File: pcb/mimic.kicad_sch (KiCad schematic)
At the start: 10 parts

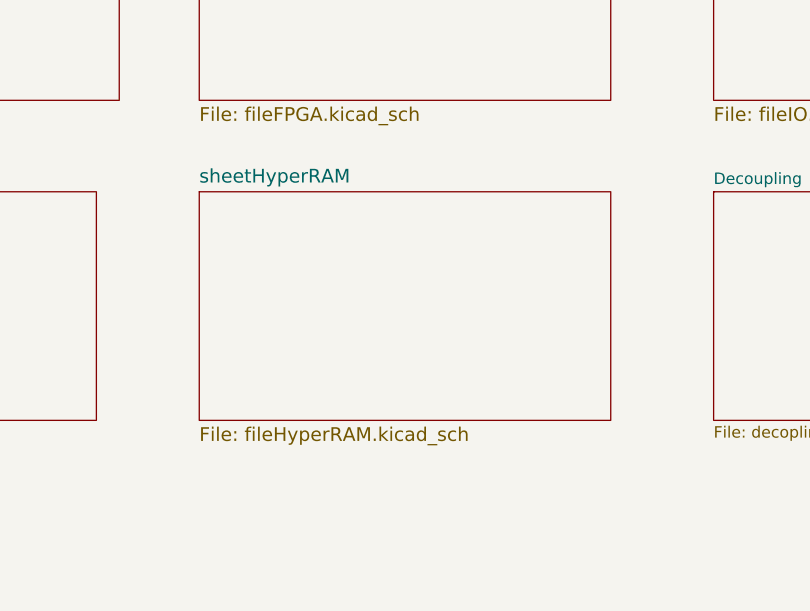
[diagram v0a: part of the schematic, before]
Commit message: refactor(pcb): strip down
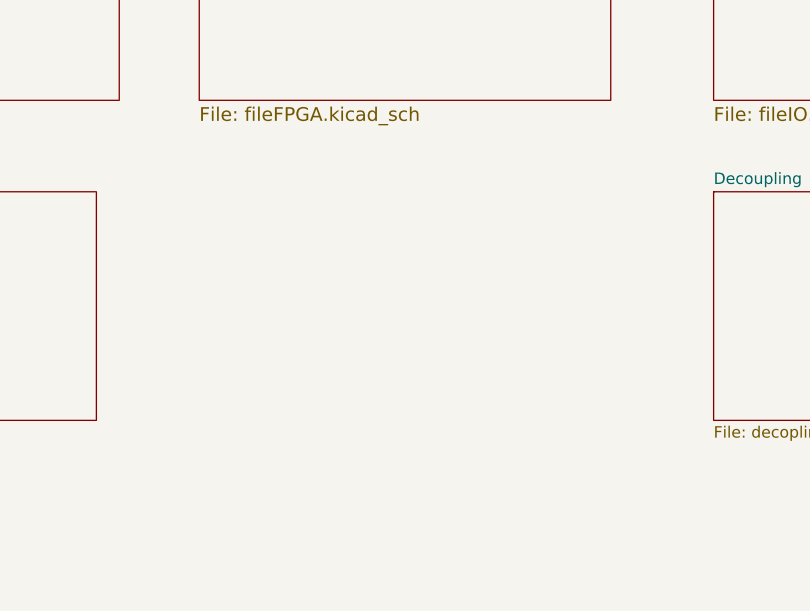
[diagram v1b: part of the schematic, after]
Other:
- removed sheet sheetHyperRAM
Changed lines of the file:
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@@
-	)
-	(sheet
-		(at 102.87 106.68)
-		(size 45.72 25.4)
-		(exclude_from_sim no)
-		(in_bom yes)
-		(on_board yes)
-		(dnp no)
-		(fields_autoplaced yes)
-		(stroke
-			(width 0)
-			(type solid)
-		)
-		(fill
-			(color 0 0 0 0)
-		)
-		(property "Sheetname" "sheetHyperRAM"
-			(at 102.87 105.8414 0)
-			(show_name no)
-			(do_not_autoplace no)
-			(effects
-				(font
-					(size 1.524 1.524)
-				)
-				(justify left bottom)
-			)
-		)
-		(property "Sheetfile" "fileHyperRAM.kicad_sch"
-			(at 102.87 132.7662 0)
-			(show_name no)
-			(do_not_autoplace no)
-			(effects
-				(font
-					(size 1.524 1.524)
-				)
-				(justify left top)
-			)
-		)
-		(instances
-			(project "mimic"
-				(path "/a721fc77-faad-4442-9d2d-3560b8c1253d"
-					(page "5")
-				)
-			)
-		)
 	)
 	(sheet
